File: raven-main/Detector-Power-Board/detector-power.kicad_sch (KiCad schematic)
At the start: 28 parts, among them J1 DeployLipo, J2 Conn_01x06, J9 UCLipo, U1 LT8330IS6-TRMPBF, U7 TPS7A4701xRGW, U8 TPS7A4701xRGW

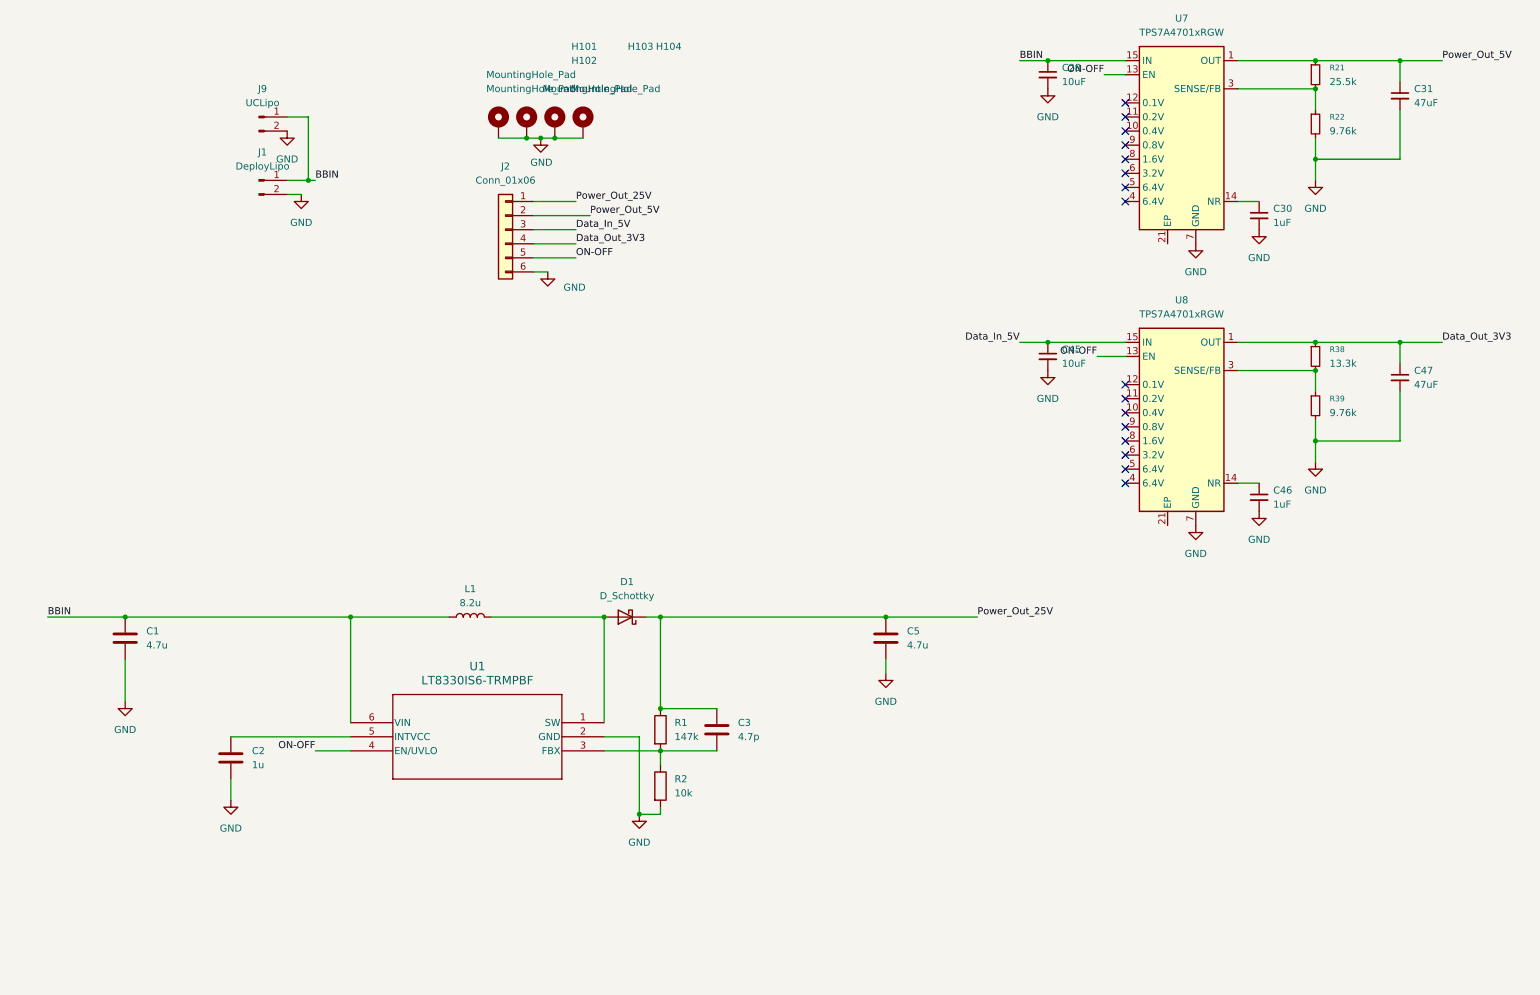
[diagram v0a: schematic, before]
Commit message: Added LDO on 25V rail
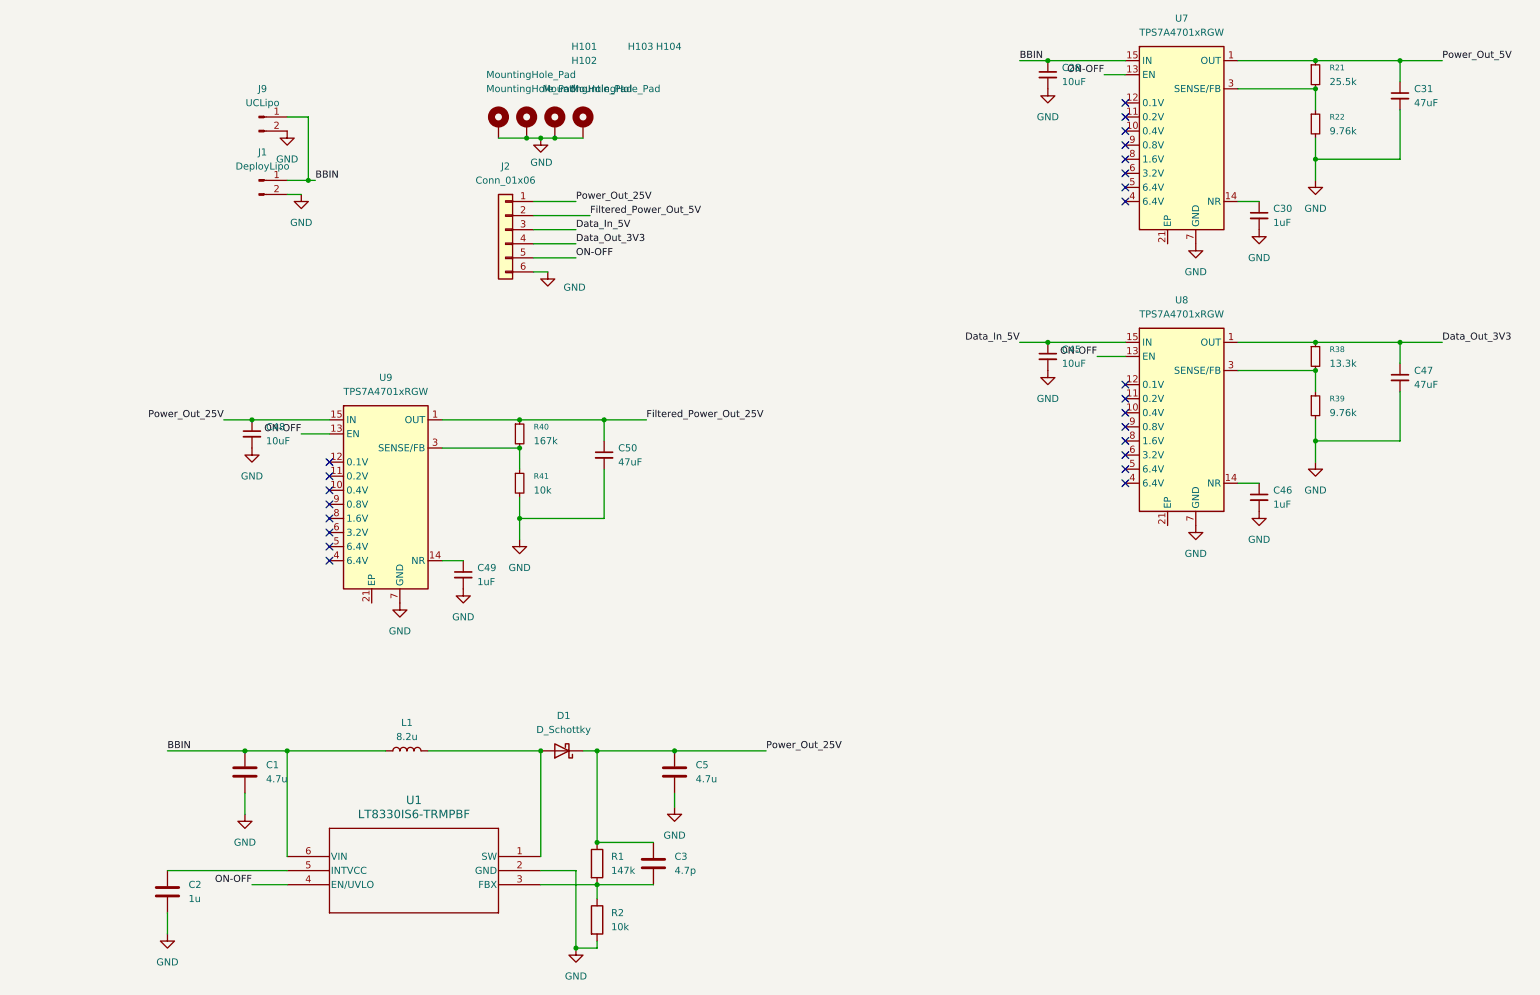
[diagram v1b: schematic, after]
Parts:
- added C48: 10uF, Capacitor_SMD:C_0805_2012Metric, symbol Device:C_Small
- added C49: 1uF, Capacitor_SMD:C_0805_2012Metric, symbol Device:C_Small
- added C50: 47uF, Capacitor_SMD:C_0805_2012Metric, symbol Device:C_Small
- added R40: 167k, Resistor_SMD:R_0402_1005Metric, symbol Device:R_Small
- added R41: 10k, Resistor_SMD:R_0402_1005Metric, symbol Device:R_Small
- added U9: TPS7A4701xRGW, Package_DFN_QFN:Texas_RGW0020A_VQFN-20-1EP_5x5mm_P0.65mm_EP3.15x3.15mm_ThermalVias, symbol Regulator_Linear:TPS7A4701xRGW
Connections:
- net GND: now also C48.2, C49.2, C50.2, R41.2, U9.7 (GND)
- net ON-OFF: now also U9.13 (EN)
- net Power_Out_25V: now also C48.1, U9.15 (IN), U9.16 (IN)
- net Power_Out_5V: no longer J2.2 (Pin_2)
- new net: R40.2, R41.1, U9.3 (SENSE/FB)
- new net: C49.1, U9.14 (NR)
- new net Filtered_Power_Out_25V: C50.1, R40.1, U9.1 (OUT), U9.20 (OUT)
- new net Filtered_Power_Out_5V: J2.2 (Pin_2)
- no-connect marks 16 -> 24
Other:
- moved on the sheet: C1, C2, C3, C5, D1, L1, R1, R2, U1

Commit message: Fixed labels and zones
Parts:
- R1: value 147k -> 162k
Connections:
- net Filtered_Power_Out_5V is gone; now on net Power_Out_5V: J2.2 (Pin_2)
- net Filtered_Power_Out_25V: now also J2.1 (Pin_1)
- net Power_Out_25V renamed Power_Out_27.5V
- net Power_Out_27.5V: no longer J2.1 (Pin_1)
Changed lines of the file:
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@@
 		)
 	)
-	(label "Power_Out_25V"
+	(label "Power_Out_27.5V"
 		(at 50.8 86.36 180)
 		(effects
@@
 		)
 	)
-	(label "Power_Out_25V"
+	(label "Filtered_Power_Out_25V"
 		(at 114.3 46.99 0)
 		(effects
@@
 		)
 	)
-	(label "Filtered_Power_Out_5V"
+	(label "Power_Out_5V"
 		(at 116.84 49.53 0)
 		(effects
@@
 		)
 	)
-	(label "Power_Out_25V"
+	(label "Power_Out_27.5V"
 		(at 148.59 146.05 0)
 		(effects
@@
 			)
 		)
-		(property "Value" "147k"
+		(property "Value" "162k"
 			(at 120.65 167.6399 0)
 			(show_name no)

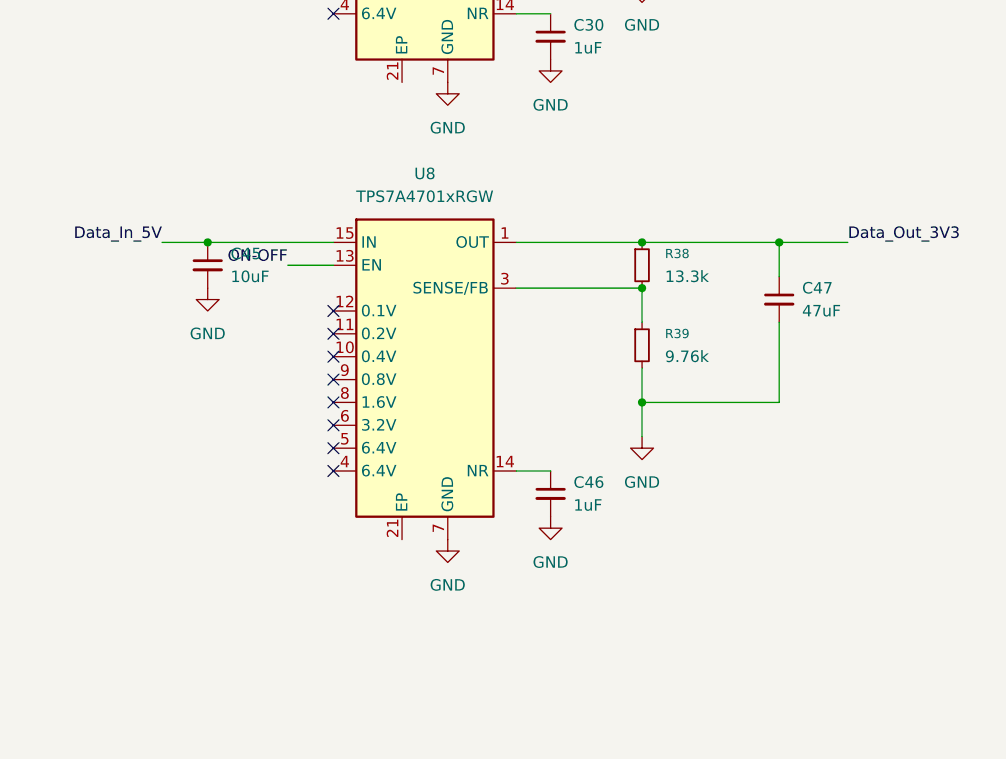
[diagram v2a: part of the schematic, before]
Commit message: Added 3.3V voltage divider to detector board
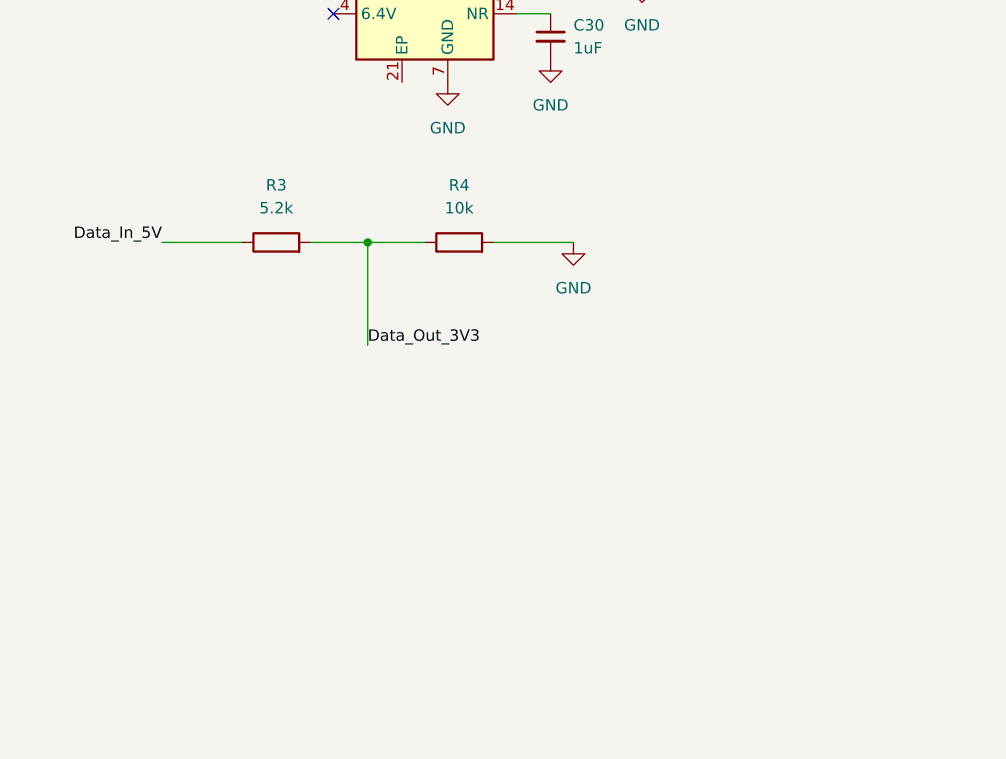
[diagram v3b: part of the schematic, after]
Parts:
- removed C45: 10uF, Capacitor_SMD:C_0805_2012Metric, symbol Device:C_Small
- removed C46: 1uF, Capacitor_SMD:C_0805_2012Metric, symbol Device:C_Small
- removed C47: 47uF, Capacitor_SMD:C_0805_2012Metric, symbol Device:C_Small
- removed R38: 13.3k, Resistor_SMD:R_0402_1005Metric, symbol Device:R_Small
- removed R39: 9.76k, Resistor_SMD:R_0402_1005Metric, symbol Device:R_Small
- removed U8: TPS7A4701xRGW, Package_DFN_QFN:Texas_RGW0020A_VQFN-20-1EP_5x5mm_P0.65mm_EP3.15x3.15mm_ThermalVias, symbol Regulator_Linear:TPS7A4701xRGW
- added R3: 5.2k, Resistor_SMD:R_0402_1005Metric, symbol Device:R
- added R4: 10k, Resistor_SMD:R_0402_1005Metric, symbol Device:R
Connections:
- net Data_In_5V: now also R3.1
- net Data_Out_3V3: now also R3.2, R4.1
- net GND: now also R4.2
- no-connect marks 24 -> 16

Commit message: Redesigned power board (again!)
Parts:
- removed C28, C48: 10uF, Capacitor_SMD:C_0805_2012Metric, symbol Device:C_Small
- removed C30, C49: 1uF, Capacitor_SMD:C_0805_2012Metric, symbol Device:C_Small
- removed C31, C50: 47uF, Capacitor_SMD:C_0805_2012Metric, symbol Device:C_Small
- removed J2: Conn_01x06, TerminalBlock_4Ucon:TerminalBlock_4Ucon_1x06_P3.50mm_Horizontal, symbol Connector_Generic:Conn_01x06
- removed R21: 25.5k, Resistor_SMD:R_0402_1005Metric, symbol Device:R_Small
- removed R22: 9.76k, Resistor_SMD:R_0402_1005Metric, symbol Device:R_Small
- removed R4: 10k, Resistor_SMD:R_0402_1005Metric, symbol Device:R
- removed R40: 167k, Resistor_SMD:R_0402_1005Metric, symbol Device:R_Small
- removed R41: 10k, Resistor_SMD:R_0402_1005Metric, symbol Device:R_Small
- removed U7, U9: TPS7A4701xRGW, Package_DFN_QFN:Texas_RGW0020A_VQFN-20-1EP_5x5mm_P0.65mm_EP3.15x3.15mm_ThermalVias, symbol Regulator_Linear:TPS7A4701xRGW
- added C10, C7, C8, C9: 1u, Capacitor_SMD:C_0805_2012Metric, symbol Device:C
- added C11: 1n, Capacitor_SMD:C_0805_2012Metric, symbol Device:C
- added C12: 5u, Capacitor_SMD:C_0805_2012Metric, symbol Device:C
- added C4, C6: 0.1u, Capacitor_SMD:C_0805_2012Metric, symbol Device:C
- added D3, D4, D5, D6: 1N4002, Diode_THT:D_DO-41_SOD81_P10.16mm_Horizontal, symbol Diode:1N4002
- added J2: Conn_01x04, Connector_PinHeader_2.54mm:PinHeader_1x04_P2.54mm_Vertical, symbol Connector_Generic:Conn_01x04
- added R4, R8: R_Variable, Resistor_SMD:R_0805_2012Metric, symbol Device:R_Variable
- added R5: 4.56k, Resistor_SMD:R_0402_1005Metric, symbol Device:R
- added R6: 240, Resistor_SMD:R_0402_1005Metric, symbol Device:R
- added R7: 720, Resistor_SMD:R_0402_1005Metric, symbol Device:R
- added U2: TPS22810DRV, Package_SON:WSON-6-1EP_2x2mm_P0.65mm_EP1x1.6mm, symbol Power_Management:TPS22810DRV
- added U3, U4: LM317LCLPRE3, LM317AMDTNOPB:TD03B_TEX, symbol LM317LCLPRE3:LM317LCLPRE3
- R3: value 5.2k -> 240
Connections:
- net Data_Out_3V3 is gone; now on net Power_Out_5V: R3.2
- net BBIN: now also C4.2, D4.1 (K), U2.1 (VOUT), U2.2 (QOD), U3.1 (INPUT); no longer J1.1 (Pin_1), J9.1 (Pin_1)
- net Filtered_Power_Out_25V: now also C8.2, D5.2 (A), D6.1 (K), J2.1 (Pin_1), R6.2, U4.2 (OUTPUT)
- net GND: now also C10.1, C11.2, C12.2, C4.1, C6.1, C7.1, C8.1, C9.1, J2.4 (Pin_4), R4.1, R8.1
- net ON-OFF: now also J2.3 (Pin_3), U2.5 (EN/UVLO); no longer U1.4 (EN/UVLO)
- net Power_Out_27.5V: now also C6.2, D5.1 (K), U4.1 (INPUT)
- net Power_Out_5V: now also C7.2, D3.1 (K), D4.2 (A), J2.2 (Pin_2), U3.2 (OUTPUT)
- net at C2.1, U1.5 (INTVCC): now also U1.4 (EN/UVLO)
- net Data_In_5V: no longer names the net of R3.1
- net Data_In_5V: now also C9.2, D3.2 (A), R4.2, U3.3 (ADJUSTMENT)
- new net: C11.1, U2.3 (CT)
- new net: C10.2, D6.2 (A), R6.1, R8.2, U4.3 (ADJUSTMENT)
- new net: C12.1, J1.1 (Pin_1), J9.1 (Pin_1), U2.6 (VIN)
- new net: U2.4 (GND), U2.7 (GND)
- no-connect marks 16 -> 0
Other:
- moved on the sheet: J1, J9
